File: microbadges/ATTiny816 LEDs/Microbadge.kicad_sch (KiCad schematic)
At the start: 15 parts, among them U1 ATtiny816-M

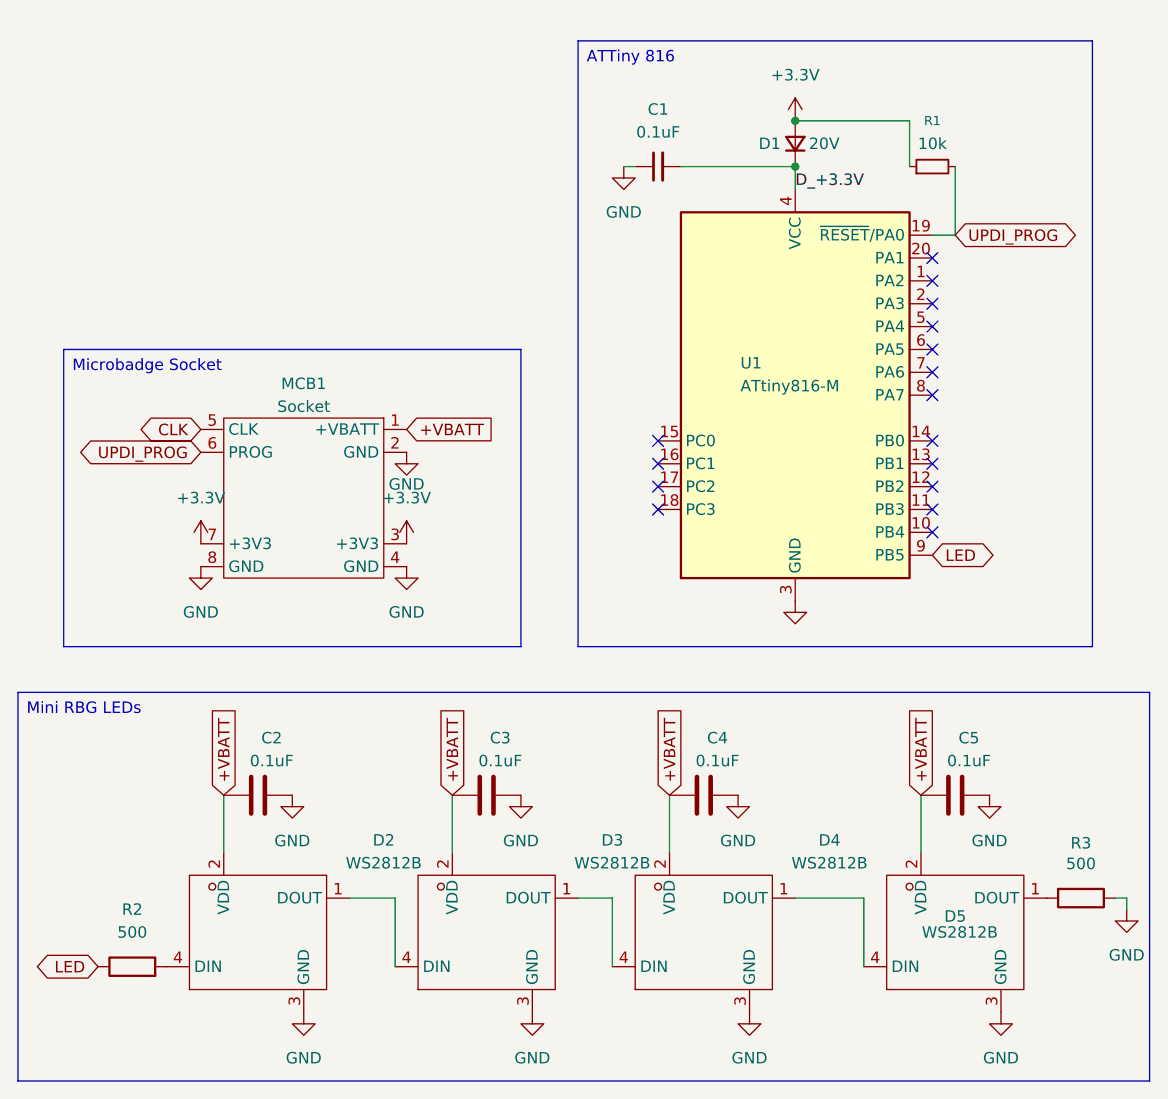
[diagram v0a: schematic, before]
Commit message: Update ATTiny Voltage to use +VBATT instead of +3V3
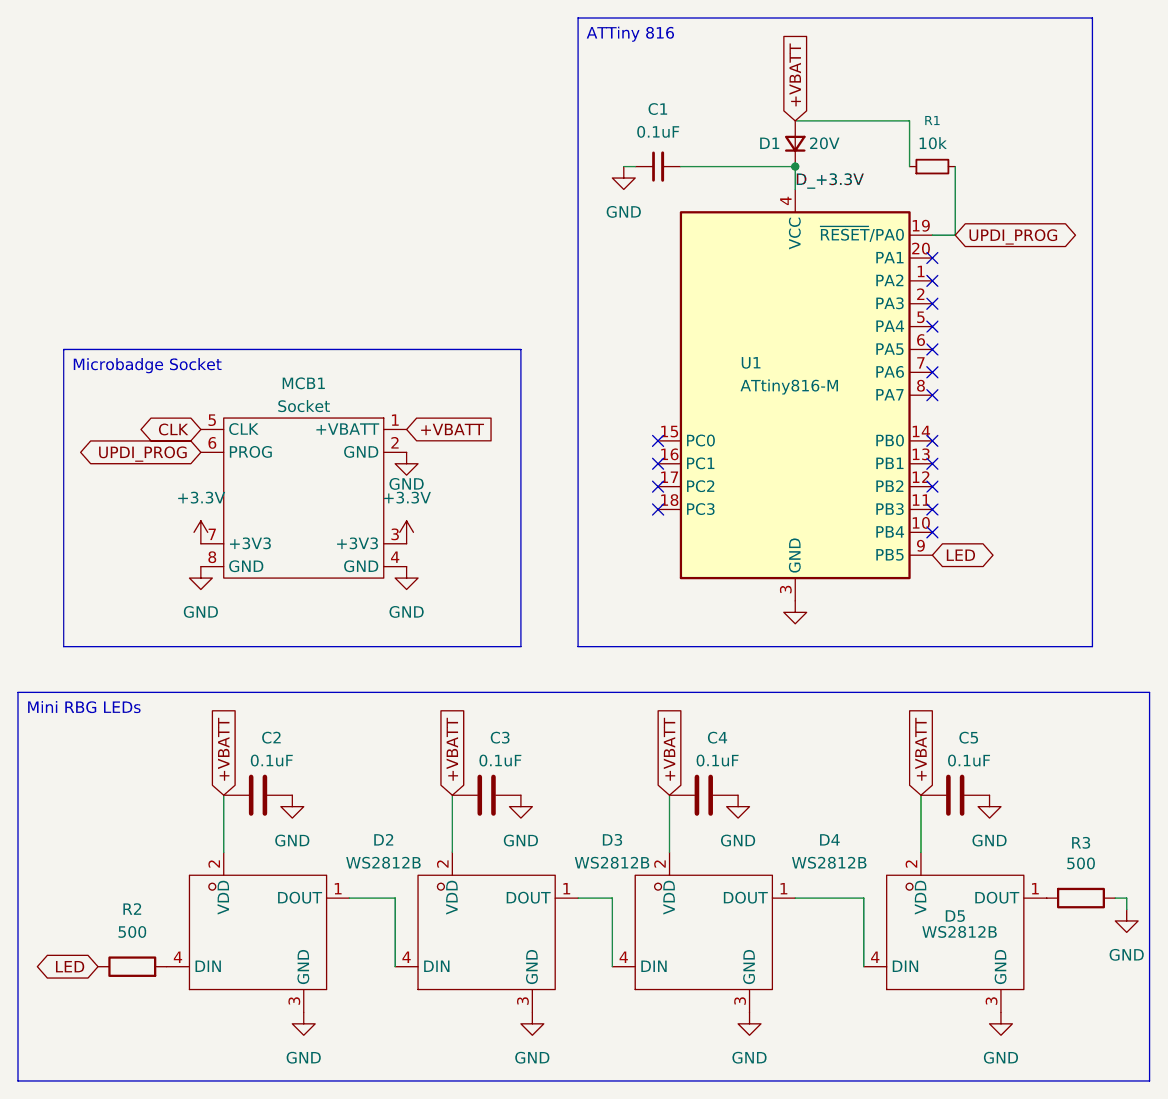
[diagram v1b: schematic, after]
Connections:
- net +3.3V: no longer D1.2 (A), R1.1
- net +VBATT: now also D1.2 (A), R1.1
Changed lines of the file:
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@@
 	(text_box "ATTiny 816"
 		(exclude_from_sim no)
-		(at 143.51 33.02 0)
-		(size 57.15 67.31)
+		(at 143.51 30.48 0)
+		(size 57.15 69.85)
 		(margins 0.9525 0.9525 0.9525 0.9525)
 		(stroke
@@
 		(color 0 0 0 0)
 	)
-	(junction
-		(at 167.64 41.91)
-		(diameter 0)
-		(color 0 0 0 0)
-	)
 	(no_connect
 		(at 182.88 64.77)
@@
 		(property "Intersheetrefs" "${INTERSHEET_REFS}"
 			(at 129.54 106.9 90)
+			(effects
+				(font
+					(size 1.27 1.27)
+				)
+				(justify left)
+				(hide yes)
+			)
+		)
+	)
+	(global_label "+VBATT"
+		(shape input)
+		(at 167.64 41.91 90)
+		(fields_autoplaced yes)
+		(effects
+			(font
+				(size 1.27 1.27)
+			)
+			(justify left)
+		)
+		(property "Intersheetrefs" "${INTERSHEET_REFS}"
+			(at 167.64 31.97 90)
 			(effects
 				(font
@@
 					(unit 1)
 				)
-			)
-		)
-	)
-	(symbol
-		(lib_id "power:+3.3V")
-		(at 167.64 41.91 0)
-		(unit 1)
-		(exclude_from_sim no)
-		(in_bom yes)
-		(on_board yes)
-		(dnp no)
-		(fields_autoplaced yes)
-		(property "Reference" "#PWR01"
-			(at 167.64 45.72 0)
-			(effects
-				(font
-					(size 1.27 1.27)
-				)
-				(hide yes)
-			)
-		)
-		(property "Value" "+3.3V"
-			(at 167.64 36.83 0)
-			(effects
-				(font
-					(size 1.27 1.27)
-				)
-			)
-		)
-		(property "Footprint" ""
-			(at 167.64 41.91 0)
-			(effects
-				(font
-					(size 1.27 1.27)
-				)
-				(hide yes)
-			)
-		)
-		(property "Datasheet" ""
-			(at 167.64 41.91 0)
-			(effects
-				(font
-					(size 1.27 1.27)
-				)
-				(hide yes)
-			)
-		)
-		(property "Description" "Power symbol creates a global label with name \"+3.3V\""
-			(at 167.64 41.91 0)
-			(effects
-				(font
-					(size 1.27 1.27)
-				)
-				(hide yes)
-			)
-		)
-		(pin "1"
-		)
-		(instances
-			(project "Microbadge"
-				(path "/5dd520c4-9ed5-468f-b7d2-9e80276de018"
-					(reference "#PWR01")
-					(unit 1)
-				)

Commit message: Fix label
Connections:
- net D_+3.3V renamed D_+VBATT
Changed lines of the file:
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@@
 		)
 	)
-	(label "D_+3.3V"
+	(label "D_+VBATT"
 		(at 167.64 49.53 0)
 		(effects

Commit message: Update Microbadge.kicad_sch
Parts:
- MCB1: footprint Microbadge:Microbadge_round -> Microbadge V2:Microbadge_V2_simple_round; symbol Pips Lib:Microbadge -> Microbadge V2:Microbadge_V2_simple; now in the parts list
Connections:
- net +3.3V: now also MCB1.11 (+3V3), MCB1.5 (+3V3); no longer MCB1.3 (+3V3), MCB1.7 (+3V3)
- net CLK: now also MCB1.7 (CLK); no longer MCB1.5 (CLK)
- net GND: now also MCB1.12 (GND), MCB1.6 (GND); no longer MCB1.4 (GND), MCB1.8 (GND)
- net UPDI_PROG: now also MCB1.8 (UPDI); no longer MCB1.6 (PROG)
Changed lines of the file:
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@@
 	(global_label "CLK"
 		(shape bidirectional)
-		(at 101.6 76.2 180)
+		(at 101.6 77.47 180)
 		(fields_autoplaced yes)
 		(effects
@@
 		)
 		(property "Intersheetrefs" "${INTERSHEET_REFS}"
-			(at 93.9354 76.2 0)
+			(at 93.9354 77.47 0)
 			(effects
 				(font
@@
 	(global_label "+VBATT"
 		(shape input)
-		(at 124.46 76.2 0)
+		(at 124.46 77.47 0)
 		(fields_autoplaced yes)
 		(effects
@@
 		)
 		(property "Intersheetrefs" "${INTERSHEET_REFS}"
-			(at 134.4 76.2 0)
+			(at 134.4 77.47 0)
 			(effects
 				(font
@@
 	(global_label "UPDI_PROG"
 		(shape bidirectional)
-		(at 101.6 78.74 180)
+		(at 101.6 80.01 180)
 		(fields_autoplaced yes)
 		(effects
@@
 		)
 		(property "Intersheetrefs" "${INTERSHEET_REFS}"
-			(at 86.9201 78.74 0)
+			(at 86.9201 80.01 0)
 			(effects
 				(font
@@
 	(symbol
 		(lib_id "power:GND")
-		(at 124.46 78.74 0)
+		(at 124.46 80.01 0)
 		(unit 1)
 		(exclude_from_sim no)
@@
 		(dnp no)
 		(property "Reference" "#PWR07"
-			(at 124.46 85.09 0)
+			(at 124.46 86.36 0)
 			(effects
 				(font
@@
 		)
 		(property "Value" "GND"
-			(at 124.46 82.296 0)
+			(at 127.762 81.788 0)
 			(effects
 				(font
@@
 		)
 		(property "Footprint" ""
-			(at 124.46 78.74 0)
+			(at 124.46 80.01 0)
 			(effects
 				(font
@@
 		)
 		(property "Datasheet" ""
-			(at 124.46 78.74 0)
+			(at 124.46 80.01 0)
 			(effects
 				(font
@@
 		)
 		(property "Description" "Power symbol creates a global label with name \"GND\" , ground"
-			(at 124.46 78.74 0)
+			(at 124.46 80.01 0)
 			(effects
 				(font
@@
 	(symbol
 		(lib_id "power:GND")
-		(at 101.6 91.44 0)
-		(unit 1)
-		(exclude_from_sim no)
-		(in_bom yes)
-		(on_board yes)
-		(dnp no)
-		(fields_autoplaced yes)
+		(at 101.6 90.17 0)
+		(unit 1)
+		(exclude_from_sim no)
+		(in_bom yes)
+		(on_board yes)
+		(dnp no)
 		(property "Reference" "#PWR013"
-			(at 101.6 97.79 0)
+			(at 101.6 96.52 0)
 			(effects
 				(font
@@
 		)
 		(property "Value" "GND"
-			(at 101.6 96.52 0)
+			(at 101.6 93.98 0)
 			(effects
 				(font
@@
 		)
 		(property "Footprint" ""
-			(at 101.6 91.44 0)
+			(at 101.6 90.17 0)
 			(effects
 				(font
@@
 		)
 		(property "Datasheet" ""
-			(at 101.6 91.44 0)
+			(at 101.6 90.17 0)
 			(effects
 				(font
@@
 		)
 		(property "Description" "Power symbol creates a global label with name \"GND\" , ground"
-			(at 101.6 91.44 0)
+			(at 101.6 90.17 0)
 			(effects
 				(font
@@
 	(symbol
 		(lib_id "power:+3.3V")
-		(at 124.46 88.9 0)
-		(unit 1)
-		(exclude_from_sim no)
-		(in_bom yes)
-		(on_board yes)
-		(dnp no)
-		(fields_autoplaced yes)
+		(at 124.46 87.63 0)
+		(unit 1)
+		(exclude_from_sim no)
+		(in_bom yes)
+		(on_board yes)
+		(dnp no)
 		(property "Reference" "#PWR04"
-			(at 124.46 92.71 0)
+			(at 124.46 91.44 0)
 			(effects
 				(font
@@
 		)
 		(property "Value" "+3.3V"
-			(at 124.46 83.82 0)
+			(at 128.016 86.614 0)
 			(effects
 				(font
@@
 		)
 		(property "Footprint" ""
-			(at 124.46 88.9 0)
+			(at 124.46 87.63 0)
 			(effects
 				(font
@@
 		)
 		(property "Datasheet" ""
-			(at 124.46 88.9 0)
+			(at 124.46 87.63 0)
 			(effects
 				(font
@@
 		)
 		(property "Description" "Power symbol creates a global label with name \"+3.3V\""
-			(at 124.46 88.9 0)
+			(at 124.46 87.63 0)
 			(effects
 				(font
@@
 	(symbol
 		(lib_id "power:GND")
-		(at 124.46 91.44 0)
-		(unit 1)
-		(exclude_from_sim no)
-		(in_bom yes)
-		(on_board yes)
-		(dnp no)
-		(fields_autoplaced yes)
+		(at 124.46 90.17 0)
+		(unit 1)
+		(exclude_from_sim no)
+		(in_bom yes)
+		(on_board yes)
+		(dnp no)
 		(property "Reference" "#PWR015"
-			(at 124.46 97.79 0)
+			(at 124.46 96.52 0)
 			(effects
 				(font
@@
 		)
 		(property "Value" "GND"
-			(at 124.46 96.52 0)
+			(at 124.46 93.98 0)
 			(effects
 				(font
@@
 		)
 		(property "Footprint" ""
-			(at 124.46 91.44 0)
+			(at 124.46 90.17 0)
 			(effects
 				(font
@@
 		)
 		(property "Datasheet" ""
-			(at 124.46 91.44 0)
+			(at 124.46 90.17 0)
 			(effects
 				(font
@@
 		)
 		(property "Description" "Power symbol creates a global label with name \"GND\" , ground"
-			(at 124.46 91.44 0)
+			(at 124.46 90.17 0)
 			(effects
 				(font
@@
 	)
 	(symbol
-		(lib_id "Pips Lib:Microbadge")
+		(lib_id "Microbadge V2:Microbadge_V2_simple")
 		(at 113.03 83.82 270)
 		(unit 1)
 		(exclude_from_sim no)
-		(in_bom no)
+		(in_bom yes)
 		(on_board yes)
 		(dnp no)
 		(fields_autoplaced yes)
 		(property "Reference" "MCB1"
-			(at 113.03 71.12 90)
+			(at 113.03 69.85 90)
 			(effects
 				(font
@@
 		)
 		(property "Value" "Socket"
-			(at 113.03 73.66 90)
-			(effects
-				(font
-					(size 1.27 1.27)
-				)
-			)
-		)
-		(property "Footprint" "Microbadge:Microbadge_round"
+			(at 113.03 72.39 90)
+			(effects
+				(font
+					(size 1.27 1.27)
+				)
+			)
+		)
+		(property "Footprint" "Microbadge V2:Microbadge_V2_simple_round"
 			(at 113.03 83.82 0)
 			(effects
@@
 			)
 		)
-		(property "Description" ""
-			(at 113.03 83.82 0)
-			(effects
-				(font
-					(size 1.27 1.27)
+		(property "Description" "SAINTCON Microbadge V2"
+			(at 111.252 83.82 0)
+			(effects
+				(font
+					(size 0.635 0.635)
 				)
 				(hide yes)
@@
 		(pin "6"
 		)
-		(pin "4"
-		)
-		(pin "3"
+		(pin "12"
+		)
+		(pin "11"
 		)
 		(pin "2"
@@
 	(symbol
 		(lib_id "power:+3.3V")
-		(at 101.6 88.9 0)
-		(unit 1)
-		(exclude_from_sim no)
-		(in_bom yes)
-		(on_board yes)
-		(dnp no)
-		(fields_autoplaced yes)
+		(at 101.6 87.63 0)
+		(unit 1)
+		(exclude_from_sim no)
+		(in_bom yes)
+		(on_board yes)
+		(dnp no)
 		(property "Reference" "#PWR06"
-			(at 101.6 92.71 0)
+			(at 101.6 91.44 0)
 			(effects
 				(font
@@
 		)
 		(property "Value" "+3.3V"
-			(at 101.6 83.82 0)
+			(at 97.79 86.868 0)
 			(effects
 				(font
@@
 		)
 		(property "Footprint" ""
-			(at 101.6 88.9 0)
+			(at 101.6 87.63 0)
 			(effects
 				(font
@@
 		)
 		(property "Datasheet" ""
-			(at 101.6 88.9 0)
+			(at 101.6 87.63 0)
 			(effects
 				(font
@@
 		)
 		(property "Description" "Power symbol creates a global label with name \"+3.3V\""
-			(at 101.6 88.9 0)
-			(effects
-				(font
+			(at 101.6 87.63 0)
+			(effects
+				(font

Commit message: Update Microbadge to V2 design
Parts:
- removed R2, R3: 500, Resistor_SMD:R_0201_0603Metric, symbol Device:R
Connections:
- net LED: now also D2.4 (DIN)
- net +3.3V: no longer names the net of MCB1.11 (+3V3)
- net +3.3V: no longer MCB1.5 (+3V3)
- no-connect marks 16 -> 19

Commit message: rotate Resistor
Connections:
- net +VBATT: now also R1.2; no longer R1.1
- net UPDI_PROG: now also R1.1; no longer R1.2
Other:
- moved on the sheet: R1
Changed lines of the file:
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@@
 	(wire
 		(pts
-			(xy 180.34 41.91) (xy 180.34 46.99)
+			(xy 123.19 128.27) (xy 123.19 135.89)
 		)
 		(stroke
@@
 	(wire
 		(pts
-			(xy 167.64 41.91) (xy 180.34 41.91)
+			(xy 185.42 44.45) (xy 185.42 41.91)
 		)
 		(stroke
@@
 	(wire
 		(pts
-			(xy 123.19 128.27) (xy 123.19 135.89)
+			(xy 104.14 116.84) (xy 104.14 123.19)
 		)
 		(stroke
@@
 	(wire
 		(pts
-			(xy 104.14 116.84) (xy 104.14 123.19)
+			(xy 147.32 128.27) (xy 147.32 135.89)
 		)
 		(stroke
@@
 	(wire
 		(pts
-			(xy 147.32 128.27) (xy 147.32 135.89)
+			(xy 185.42 54.61) (xy 182.88 54.61)
 		)
 		(stroke
@@
 	(wire
 		(pts
-			(xy 185.42 54.61) (xy 182.88 54.61)
+			(xy 129.54 116.84) (xy 129.54 123.19)
 		)
 		(stroke
@@
 	(wire
 		(pts
-			(xy 129.54 116.84) (xy 129.54 123.19)
+			(xy 181.61 116.84) (xy 181.61 123.19)
 		)
 		(stroke
@@
 	(wire
 		(pts
-			(xy 181.61 116.84) (xy 181.61 123.19)
+			(xy 154.94 46.99) (xy 167.64 46.99)
 		)
 		(stroke
@@
 	(wire
 		(pts
-			(xy 154.94 46.99) (xy 167.64 46.99)
+			(xy 143.51 128.27) (xy 147.32 128.27)
 		)
 		(stroke
@@
 	(wire
 		(pts
-			(xy 143.51 128.27) (xy 147.32 128.27)
+			(xy 118.11 128.27) (xy 123.19 128.27)
 		)
 		(stroke
@@
 	(wire
 		(pts
-			(xy 118.11 128.27) (xy 123.19 128.27)
+			(xy 185.42 41.91) (xy 167.64 41.91)
 		)
 		(stroke
@@
 	(wire
 		(pts
-			(xy 185.42 46.99) (xy 185.42 54.61)
+			(xy 185.42 49.53) (xy 185.42 54.61)
 		)
 		(stroke
@@
 	(symbol
 		(lib_id "Device:R_Small")
-		(at 182.88 46.99 90)
+		(at 185.42 46.99 180)
 		(unit 1)
 		(exclude_from_sim no)
@@
 		(fields_autoplaced yes)
 		(property "Reference" "R1"
-			(at 182.88 41.91 90)
+			(at 187.96 45.7199 0)
 			(effects
 				(font
 					(size 1.016 1.016)
 				)
+				(justify right)
 			)
 		)
 		(property "Value" "10k"
-			(at 182.88 44.45 90)
-			(effects
-				(font
-					(size 1.27 1.27)
-				)
+			(at 187.96 48.2599 0)
+			(effects
+				(font
+					(size 1.27 1.27)
+				)
+				(justify right)
 			)
 		)
 		(property "Footprint" "Resistor_SMD:R_0201_0603Metric"
-			(at 182.88 46.99 0)
+			(at 185.42 46.99 0)
 			(effects
 				(font
@@
 		)
 		(property "Datasheet" "~"
-			(at 182.88 46.99 0)
+			(at 185.42 46.99 0)
 			(effects
 				(font
@@
 		)
 		(property "Description" "Resistor, small symbol"
-			(at 182.88 46.99 0)
-			(effects
-				(font
+			(at 185.42 46.99 0)
+			(effects
+				(font

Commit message: Add LCSC part numbers to components
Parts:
- C1, C2, C3, C4, C5: LCSC Part # (none) -> C49062
- D1: LCSC Part # (none) -> C552803
- D2, D3, D4, D5: LCSC Part # (none) -> C5349953
- MCB1: now left out of the parts list
- R1: LCSC Part # (none) -> C100126
- U1: LCSC Part # (none) -> C2052778
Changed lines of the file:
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@@
+			)
+		)
+		(property "LCSC Part #" "C49062"
+			(at 107.95 116.84 90)
+			(effects
+				(font
+					(size 1.27 1.27)
+				)
+				(hide yes)
 			)
 		)
@@
 			)
 		)
+		(property "LCSC Part #" "C49062"
+			(at 133.35 116.84 90)
+			(effects
+				(font
+					(size 1.27 1.27)
+				)
+				(hide yes)
+			)
+		)
 		(pin "2"
 		)
@@
 			)
 		)
+		(property "LCSC Part #" "C5349953"
+			(at 157.48 132.08 0)
+			(effects
+				(font
+					(size 1.27 1.27)
+				)
+				(hide yes)
+			)
+		)
 		(pin "1"
 		)
@@
 			)
 		)
+		(property "LCSC Part #" "C5349953"
+			(at 107.95 132.08 0)
+			(effects
+				(font
+					(size 1.27 1.27)
+				)
+				(hide yes)
+			)
+		)
 		(pin "1"
 		)
@@
 		(unit 1)
 		(exclude_from_sim no)
-		(in_bom yes)
+		(in_bom no)
 		(on_board yes)
 		(dnp no)
@@
 			)
 		)
+		(property "LCSC Part #" "C49062"
+			(at 157.48 116.84 90)
+			(effects
+				(font
+					(size 1.27 1.27)
+				)
+				(hide yes)
+			)
+		)
 		(pin "2"
 		)
@@
 			)
 		)
+		(property "LCSC Part #" "C2052778"
+			(at 167.64 72.39 0)
+			(effects
+				(font
+					(size 1.27 1.27)
+				)
+				(hide yes)
+			)
+		)
 		(pin "15"
 		)
@@
 		(property "Sim.Pins" "1=K 2=A"
 			(at 167.64 44.45 0)
+			(effects
+				(font
+					(size 1.27 1.27)
+				)
+				(hide yes)
+			)
+		)
+		(property "LCSC Part #" "C552803"
+			(at 167.64 44.45 90)
 			(effects
 				(font
@@
 			)
 		)
+		(property "LCSC Part #" "C49062"
+			(at 152.4 46.99 90)
+			(effects
+				(font
+					(size 1.27 1.27)
+				)
+				(hide yes)
+			)
+		)
 		(pin "1"
 		)
@@
 		)
 		(property "LCSC Part Name" "XL-1010RGBC-WS2812B"
+			(at 185.42 132.08 0)
+			(effects
+				(font
+					(size 1.27 1.27)
+				)
+				(hide yes)
+			)
+		)
+		(property "LCSC Part #" "C5349953"
 			(at 185.42 132.08 0)
 			(effects
@@
 			)
 		)
+		(property "LCSC Part #" "C49062"
+			(at 185.42 116.84 90)
+			(effects
+				(font
+					(size 1.27 1.27)
+				)
+				(hide yes)
+			)
+		)
 		(pin "2"
 		)
@@
 			)
 		)
+		(property "LCSC Part #" "C100126"
+			(at 185.42 46.99 0)
+			(effects
+				(font
+					(size 1.27 1.27)
+				)
+				(hide yes)
+			)
+		)
 		(pin "1"
 		)
@@
 			(at 133.35 132.08 0)
 			(effects
+				(font
+					(size 1.27 1.27)
+				)
+				(hide yes)
+			)
+		)
+		(property "LCSC Part #" "C5349953"
+			(at 133.35 132.08 0)
+			(effects

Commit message: Update to Bit-banged I2C
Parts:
- MCB1: footprint Microbadge V2:Microbadge_V2_simple_round -> Microbadge V2:Microbadge_V2_full_round; symbol Microbadge V2:Microbadge_V2_simple -> Microbadge V2:Microbadge_V2_full; now in the parts list
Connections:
- net SDA: now reaches U1.15 (PC0)
- net SDA: now also MCB1.10 (SDA)
- net SCL: now reaches U1.16 (PC1)
- net SCL: now also MCB1.9 (SCL)
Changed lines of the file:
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@@
+	)
+	(no_connect
+		(at 124.46 82.55)
+	)
+	(no_connect
+		(at 124.46 85.09)
 	)
 	(no_connect
@@
 	)
 	(no_connect
-		(at 152.4 80.01)
-	)
-	(no_connect
 		(at 182.88 69.85)
 	)
@@
 	(no_connect
 		(at 195.58 128.27)
-	)
-	(no_connect
-		(at 152.4 77.47)
 	)
 	(no_connect
@@
 		)
 	)
+	(global_label "SDA"
+		(shape bidirectional)
+		(at 152.4 77.47 180)
+		(fields_autoplaced yes)
+		(effects
+			(font
+				(size 1.27 1.27)
+			)
+			(justify right)
+		)
+		(property "Intersheetrefs" "${INTERSHEET_REFS}"
+			(at 144.7354 77.47 0)
+			(effects
+				(font
+					(size 1.27 1.27)
+				)
+				(justify right)
+				(hide yes)
+			)
+		)
+	)
 	(global_label "+VBATT"
 		(shape input)
@@
 		)
 	)
+	(global_label "SDA"
+		(shape bidirectional)
+		(at 101.6 85.09 180)
+		(fields_autoplaced yes)
+		(effects
+			(font
+				(size 1.27 1.27)
+			)
+			(justify right)
+		)
+		(property "Intersheetrefs" "${INTERSHEET_REFS}"
+			(at 93.9354 85.09 0)
+			(effects
+				(font
+					(size 1.27 1.27)
+				)
+				(justify right)
+				(hide yes)
+			)
+		)
+	)
 	(global_label "UPDI_PROG"
 		(shape bidirectional)
@@
 		)
 	)
+	(global_label "SCL"
+		(shape bidirectional)
+		(at 152.4 80.01 180)
+		(fields_autoplaced yes)
+		(effects
+			(font
+				(size 1.27 1.27)
+			)
+			(justify right)
+		)
+		(property "Intersheetrefs" "${INTERSHEET_REFS}"
+			(at 144.7959 80.01 0)
+			(effects
+				(font
+					(size 1.27 1.27)
+				)
+				(justify right)
+				(hide yes)
+			)
+		)
+	)
 	(global_label "+VBATT"
 		(shape input)
@@
 				)
 				(justify left)
+				(hide yes)
+			)
+		)
+	)
+	(global_label "SCL"
+		(shape bidirectional)
+		(at 101.6 82.55 180)
+		(fields_autoplaced yes)
+		(effects
+			(font
+				(size 1.27 1.27)
+			)
+			(justify right)
+		)
+		(property "Intersheetrefs" "${INTERSHEET_REFS}"
+			(at 93.9959 82.55 0)
+			(effects
+				(font
+					(size 1.27 1.27)
+				)
+				(justify right)
 				(hide yes)
 			)
@@
 	)
 	(symbol
-		(lib_id "Microbadge V2:Microbadge_V2_simple")
+		(lib_id "Microbadge V2:Microbadge_V2_full")
 		(at 113.03 83.82 270)
 		(unit 1)
 		(exclude_from_sim no)
-		(in_bom no)
+		(in_bom yes)
 		(on_board yes)
 		(dnp no)
@@
 			)
 		)
-		(property "Footprint" "Microbadge V2:Microbadge_V2_simple_round"
+		(property "Footprint" "Microbadge V2:Microbadge_V2_full_round"
 			(at 113.03 83.82 0)
 			(effects
@@
 		(pin "2"
 		)
+		(pin "10"
+		)
+		(pin "9"
+		)
+		(pin "3"
+		)
+		(pin "4"
+		)
 		(instances
